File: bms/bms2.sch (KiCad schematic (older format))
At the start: 44 parts

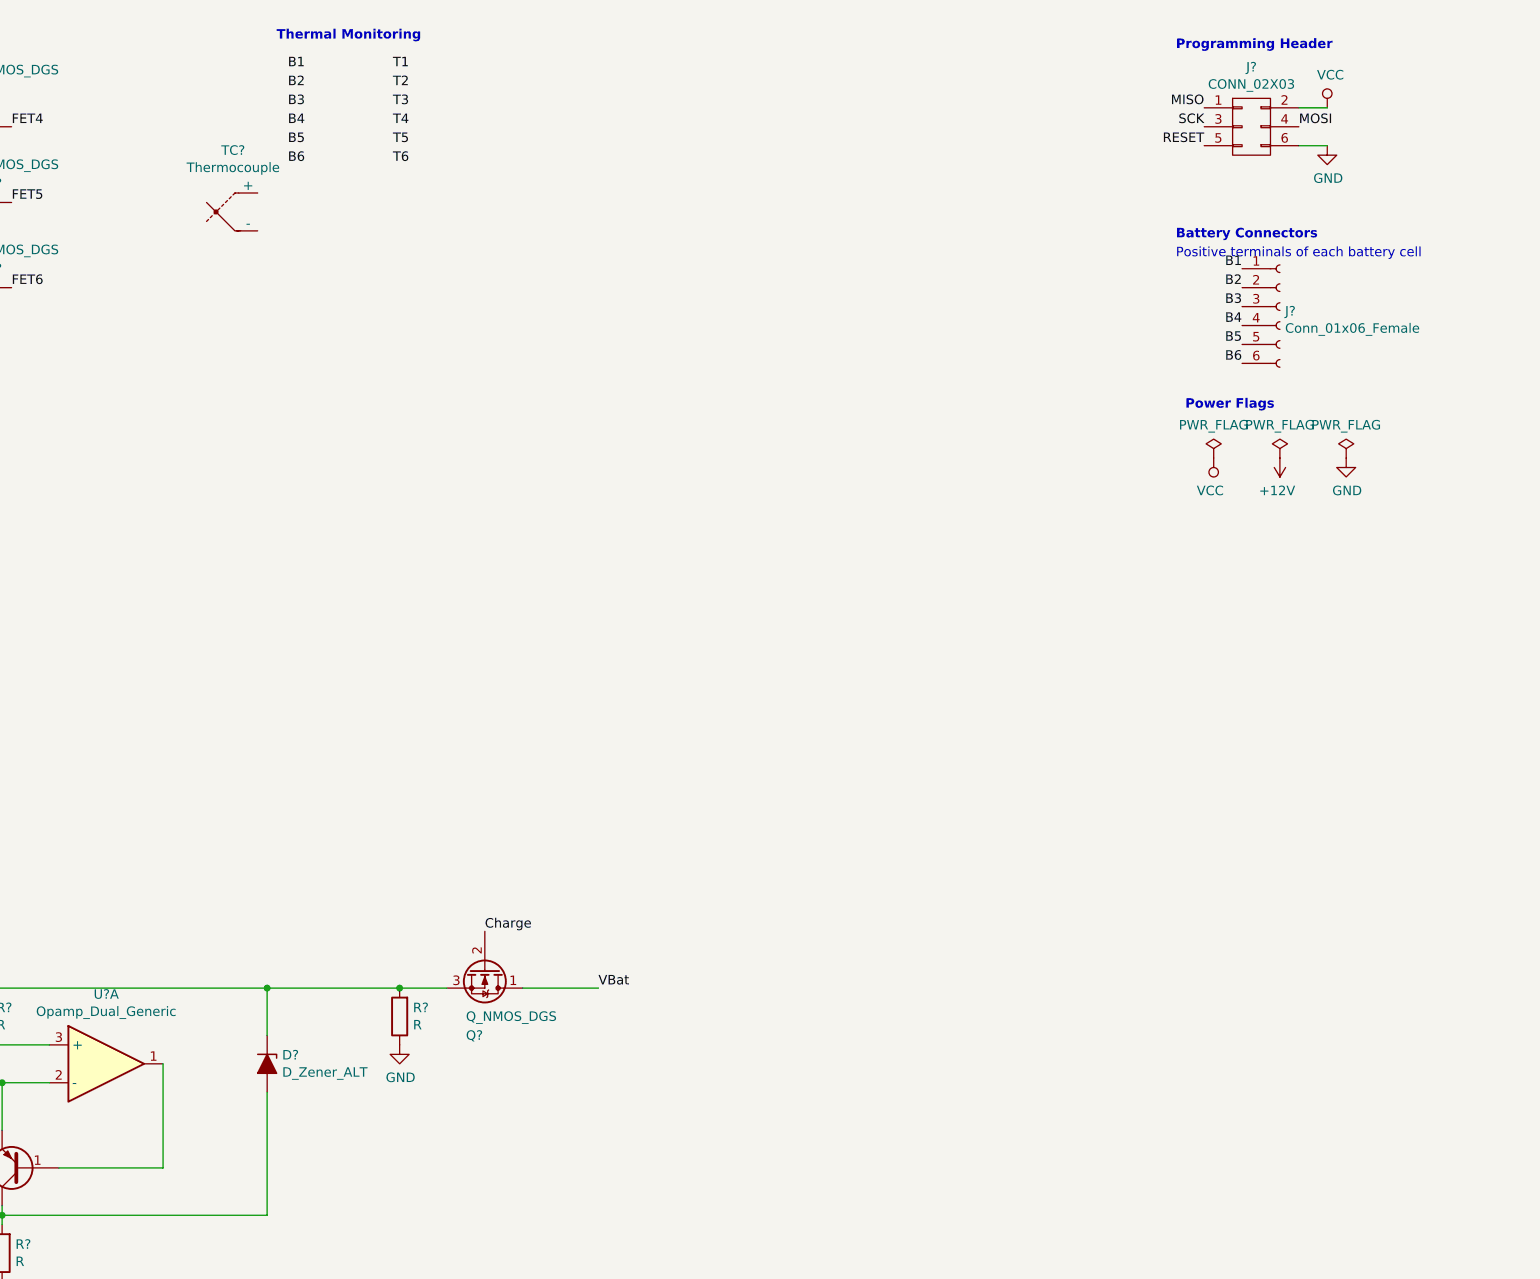
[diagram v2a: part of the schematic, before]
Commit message: thermal monitoring and eFuse safety
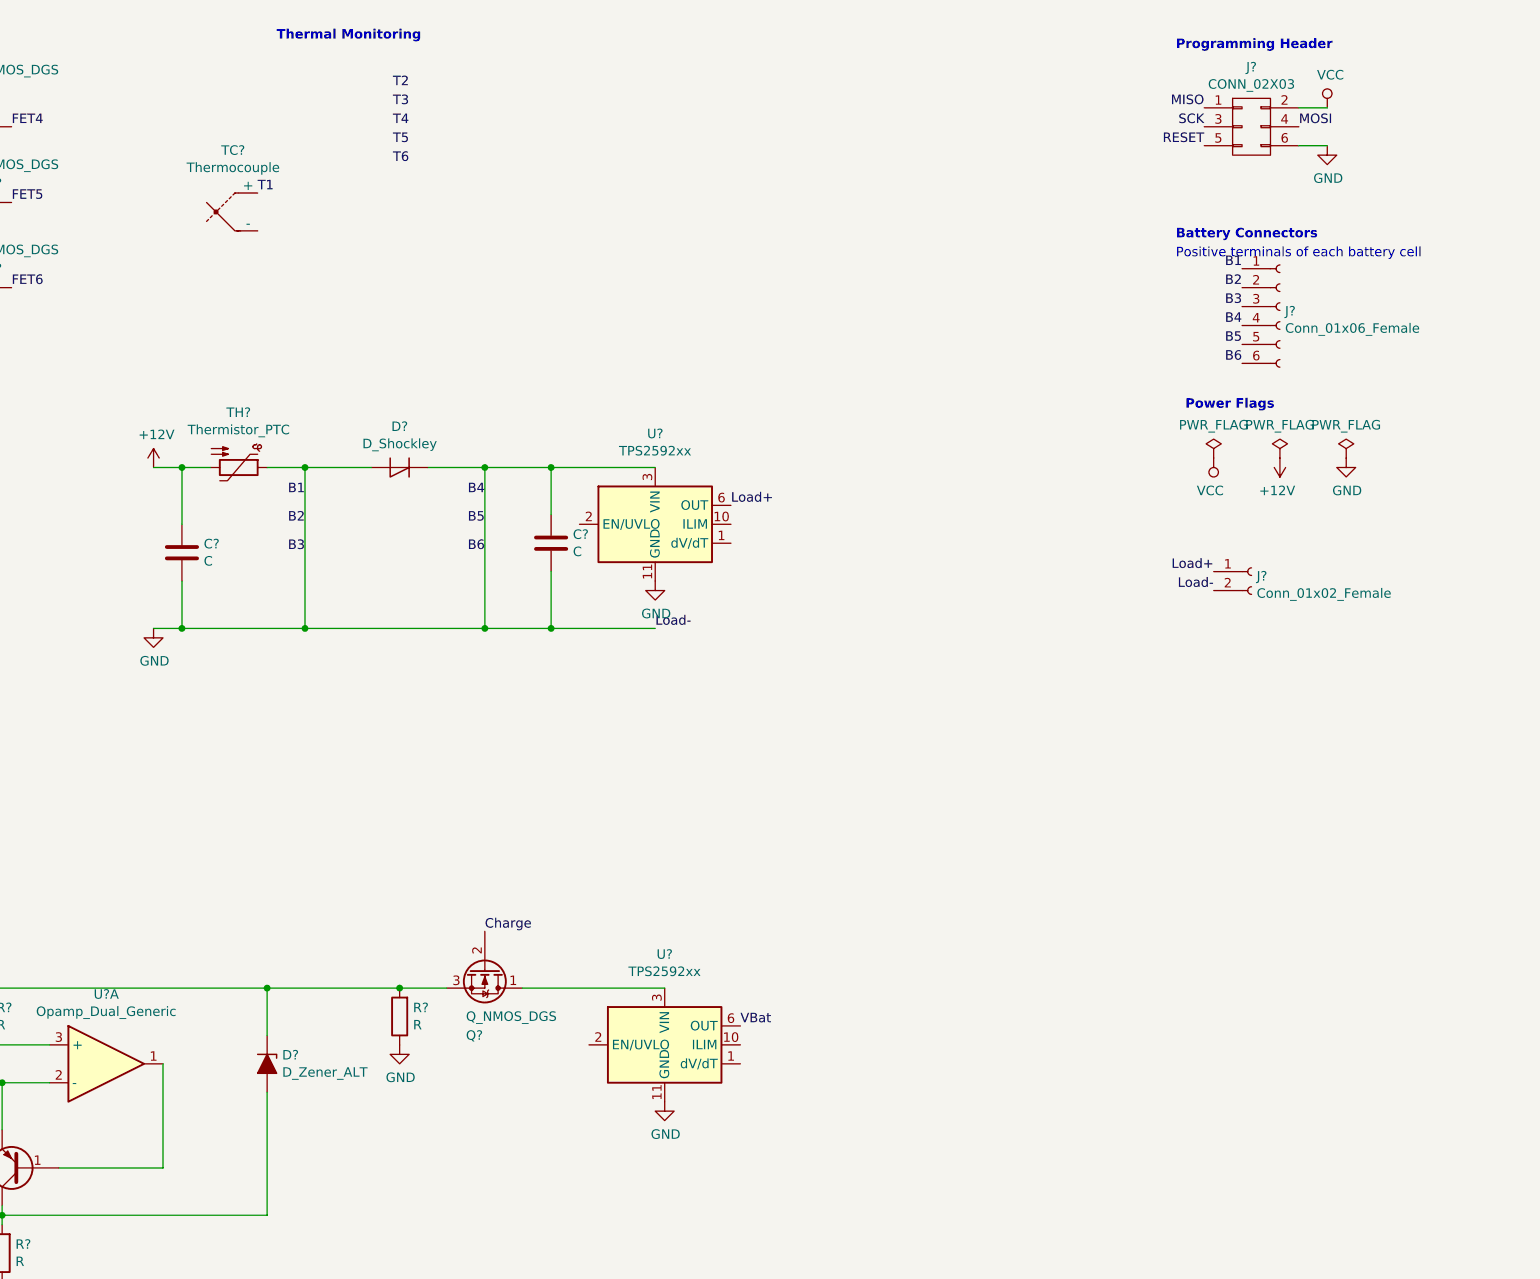
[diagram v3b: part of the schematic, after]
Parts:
- added C? (x2): C, symbol Device:C
- added D?: D_Shockley, symbol Device:D_Shockley
- added J?: Conn_01x02_Female, symbol Connector:Conn_01x02_Female
- added TH?: Thermistor_PTC, symbol Device:Thermistor_PTC
- added U? (x2): TPS2592xx, Package_SON:VSON-10-1EP_3x3mm_P0.5mm_EP1.65x2.4mm_ThermalVias, symbol Power_Management:TPS2592xx
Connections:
- net B1 is gone; now on net GND: J?.1 (Pin_1), R?.2
- net B2 is gone; now on net GND: J?.2 (Pin_2), R?.2
- net B3 is gone; now on net GND: J?.3 (Pin_3), R?.2
- net B4 is gone; now on net GND: J?.4 (Pin_4), R?.2
- net B5 is gone; now on net GND: J?.5 (Pin_5), R?.2
- net B6 is gone; now on net GND: J?.6 (Pin_6), R?.2
- net +12V: now also C?.1, TH?.2
- net GND: now also C?.1, C?.2, C?.2, D?.1 (K), D?.2 (A), J?.2 (Pin_2), TH?.1, U?.11 (GND), U?.11 (GND), U?.3 (VIN), U?.4 (VIN), U?.5 (VIN)
- net T1: now also TC?.1 (+)
- net VBat: now also U?.6 (OUT), U?.7 (OUT), U?.8 (OUT); no longer Q?.1 (D)
- new net: Q?.1 (D), U?.3 (VIN), U?.4 (VIN), U?.5 (VIN)
- new net Load+: J?.1 (Pin_1), U?.6 (OUT), U?.7 (OUT), U?.8 (OUT)
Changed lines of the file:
@@
 Text Notes 950  6450 0    50   ~ 0
 Buck Power Stage\n
-Text Label 6600 5800 0    50   ~ 0
+Text Label 7350 6000 0    50   ~ 0
 VBat
 Text Label 2450 3200 0    50   ~ 0
@@
 Text Label 6000 5500 0    50   ~ 0
 Charge
-Wire Wire Line
-	6200 5800 6600 5800
 Text Notes 4900 800  0    50   ~ 10
 Thermal Monitoring\n
@@
 Text Label 10000 2500 2    50   ~ 0
 B6
-Text Label 5050 950  2    50   ~ 0
-B1
-Text Label 5050 1050 2    50   ~ 0
-B2
-Text Label 5050 1150 2    50   ~ 0
-B3
-Text Label 5050 1250 2    50   ~ 0
-B4
-Text Label 5050 1350 2    50   ~ 0
-B5
-Text Label 5050 1450 2    50   ~ 0
-B6
-Text Label 5600 950  2    50   ~ 0
+Text Label 4800 1600 0    50   ~ 0
 T1
 Text Label 5600 1050 2    50   ~ 0
@@
 	1    0    0    -1
 $EndComp
+Text Label 5050 3200 2    50   ~ 0
+B1
+Text Label 5050 3350 2    50   ~ 0
+B2
+Text Label 5050 3500 2    50   ~ 0
+B3
+Text Label 6000 3200 2    50   ~ 0
+B4
+Text Label 6000 3350 2    50   ~ 0
+B5
+Text Label 6000 3500 2    50   ~ 0
+B6
+Wire Wire Line
+	4250 3050 4400 3050
+Wire Wire Line
+	6000 3050 6350 3050
+Wire Wire Line
+	4250 3900 4400 3900
+Wire Wire Line
+	5050 3050 5050 3900
+Connection ~ 5050 3900
+Wire Wire Line
+	5050 3900 6000 3900
+Wire Wire Line
+	6000 3050 6000 3900
+Connection ~ 6000 3900
+Wire Wire Line
+	6000 3900 6350 3900
+$Comp
+L power:+12V #PWR?
+U 1 1 5E179A7D
+P 4250 3050
+F 0 "#PWR?" H 4250 2900 50  0001 C CNN
+F 1 "+12V" H 4265 3223 50  0000 C CNN
+F 2 "" H 4250 3050 50  0001 C CNN
+F 3 "" H 4250 3050 50  0001 C CNN
+	1    4250 3050
+	1    0    0    -1
+$EndComp
+$Comp
+L power:GND #PWR?
+U 1 1 5E179C4F
+P 4250 3900
+F 0 "#PWR?" H 4250 3650 50  0001 C CNN
+F 1 "GND" H 4255 3727 50  0000 C CNN
+F 2 "" H 4250 3900 50  0001 C CNN
+F 3 "" H 4250 3900 50  0001 C CNN
+	1    4250 3900
+	1    0    0    -1
+$EndComp
+$Comp
+L Connector:Conn_01x02_Female J?
+U 1 1 5E179EB6
+P 10050 3600
+F 0 "J?" H 10077 3576 50  0000 L CNN
+F 1 "Conn_01x02_Female" H 10077 3485 50  0000 L CNN
+F 2 "" H 10050 3600 50  0001 C CNN
+F 3 "~" H 10050 3600 50  0001 C CNN
+	1    10050 3600
+	1    0    0    -1
+$EndComp
+Text Label 9850 3600 2    50   ~ 0
+Load+
+Text Label 9850 3700 2    50   ~ 0
+Load-
+Text Label 7300 3250 0    50   ~ 0
+Load+
+Text Label 6900 3900 0    50   ~ 0
+Load-
+$Comp
+L Device:D_Shockley D?
+U 1 1 5E17A7E8
+P 5550 3050
+F 0 "D?" H 5550 2834 50  0000 C CNN
+F 1 "D_Shockley" H 5550 2925 50  0000 C CNN
+F 2 "" H 5550 3050 50  0001 C CNN
+F 3 "~" H 5550 3050 50  0001 C CNN
+	1    5550 3050
+	-1   0    0    1
+$EndComp
+$Comp
+L power:GND #PWR?
+U 1 1 5E17AAB6
+P 6900 3650
+F 0 "#PWR?" H 6900 3400 50  0001 C CNN
+F 1 "GND" H 6905 3477 50  0000 C CNN
+F 2 "" H 6900 3650 50  0001 C CNN
+F 3 "" H 6900 3650 50  0001 C CNN
+	1    6900 3650
+	1    0    0    -1
+$EndComp
+$Comp
+L Power_Management:TPS2592xx U?
+U 1 1 5E17AB1F
+P 6900 3350
+F 0 "U?" H 6900 3828 50  0000 C CNN
+F 1 "TPS2592xx" H 6900 3737 50  0000 C CNN
+F 2 "Package_SON:VSON-10-1EP_3x3mm_P0.5mm_EP1.65x2.4mm_ThermalVias" H 6850 2700 50  0001 C CNN
+F 3 "http://www.ti.com/lit/ds/symlink/tps25925.pdf" H 6500 3750 50  0001 C CNN
+	1    6900 3350
+	1    0    0    -1
+$EndComp
+Wire Wire Line
+	5050 3050 5400 3050
+Wire Wire Line
+	5700 3050 6000 3050
+Connection ~ 5050 3050
+Connection ~ 6000 3050
+$Comp
+L Power_Management:TPS2592xx U?
+U 1 1 5E17D9BC
+P 6950 6100
+F 0 "U?" H 6950 6578 50  0000 C CNN
+F 1 "TPS2592xx" H 6950 6487 50  0000 C CNN
+F 2 "Package_SON:VSON-10-1EP_3x3mm_P0.5mm_EP1.65x2.4mm_ThermalVias" H 6900 5450 50  0001 C CNN
+F 3 "http://www.ti.com/lit/ds/symlink/tps25925.pdf" H 6550 6500 50  0001 C CNN
+	1    6950 6100
+	1    0    0    -1
+$EndComp
+Wire Wire Line
+	6200 5800 6950 5800
+$Comp
+L power:GND #PWR?
+U 1 1 5E1803FE
+P 6950 6400
+F 0 "#PWR?" H 6950 6150 50  0001 C CNN
+F 1 "GND" H 6955 6227 50  0000 C CNN
+F 2 "" H 6950 6400 50  0001 C CNN
+F 3 "" H 6950 6400 50  0001 C CNN
+	1    6950 6400
+	1    0    0    -1
+$EndComp
+$Comp
+L Device:C C?
+U 1 1 5E18086C
+P 4400 3500
+F 0 "C?" H 4515 3546 50  0000 L CNN
+F 1 "C" H 4515 3455 50  0000 L CNN
+F 2 "" H 4438 3350 50  0001 C CNN
+F 3 "~" H 4400 3500 50  0001 C CNN
+	1    4400 3500
+	1    0    0    -1
+$EndComp
+$Comp
+L Device:C C?
+U 1 1 5E18097C
+P 6350 3450
+F 0 "C?" H 6465 3496 50  0000 L CNN
+F 1 "C" H 6465 3405 50  0000 L CNN
+F 2 "" H 6388 3300 50  0001 C CNN
+F 3 "~" H 6350 3450 50  0001 C CNN
+	1    6350 3450
+	1    0    0    -1
+$EndComp
+$Comp
+L Device:Thermistor_PTC TH?
+U 1 1 5E180AA9
+P 4700 3050
+F 0 "TH?" V 4410 3050 50  0000 C CNN
+F 1 "Thermistor_PTC" V 4501 3050 50  0000 C CNN
+F 2 "" H 4750 2850 50  0001 L CNN
+F 3 "~" H 4700 3050 50  0001 C CNN
+	1    4700 3050
+	0    1    1    0
+$EndComp
+Wire Wire Line
+	6350 3050 6350 3300
+Wire Wire Line
+	6350 3600 6350 3900
+Connection ~ 6350 3050
+Wire Wire Line
+	6350 3050 6900 3050
+Connection ~ 6350 3900
+Wire Wire Line
+	6350 3900 6900 3900
+Wire Wire Line
+	4400 3050 4400 3350
+Wire Wire Line
+	4400 3650 4400 3900
+Connection ~ 4400 3050
+Wire Wire Line
+	4400 3050 4550 3050
+Connection ~ 4400 3900
+Wire Wire Line
+	4400 3900 5050 3900
+Wire Wire Line
+	4850 3050 5050 3050
 $EndSCHEMATC

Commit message: MAX1648 charging chip!
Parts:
- added C? (x2): CP, symbol Device:CP
- added C? (x5): C, symbol Device:C
- added D?: D_Shockley, symbol Device:D_Shockley
- added D? (x3): D_Schottky, symbol Device:D_Schottky
- added D?: D, symbol Device:D
- added L?: INDUCTOR, symbol pspice:INDUCTOR
- added M? (x2): MNMOS, symbol pspice:MNMOS
- added Q?: BS170, Package_TO_SOT_THT:TO-92_Inline, symbol Transistor_FET:BS170
- added R? (x9): R, symbol Device:R
- added TC? (x5): Thermocouple, symbol Device:Thermocouple
- added U?: ATSAMD21G18A-AUT, digikey-footprints:TQFP-48_7x7mm, symbol dk_Embedded-Microcontrollers:ATSAMD21G18A-AUT
- added U?: MAX1648, Package_SO:SOIC-16_3.9x9.9mm_P1.27mm, symbol Battery_Management:MAX1648
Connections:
- net labels added: LoadSwitch, SafetySwitch
- wire segments 99 -> 165
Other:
- note added: "Load Switch\n"
- moved on the sheet: C?, D?, J?, L?, Q?, R?, TC?, TH?, U?, U?A

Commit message: C and R values for charging circuit
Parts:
- removed C? (x3): C, symbol Device:C
- removed D?: D, symbol Device:D
- removed D?: D_Zener_ALT, symbol Device:D_Zener_ALT
- removed L?: INDUCTOR, symbol pspice:INDUCTOR
- removed Q?: Q_PNP_BCE, symbol Device:Q_PNP_BCE
- removed Q?: Q_NMOS_DGS, symbol Device:Q_NMOS_DGS
- removed Q?: BS170, Package_TO_SOT_THT:TO-92_Inline, symbol Transistor_FET:BS170
- removed R? (x5): R, symbol Device:R
- removed TC? (x6): Thermocouple, symbol Device:Thermocouple
- removed TH?: Thermistor_PTC, symbol Device:Thermistor_PTC
- removed U?: Opamp_Dual_Generic, symbol Device:Opamp_Dual_Generic
- removed U?: TPS2592xx, Package_SON:VSON-10-1EP_3x3mm_P0.5mm_EP1.65x2.4mm_ThermalVias, symbol Power_Management:TPS2592xx
- added C10: 0.1uF, Capacitor_SMD:C_0805_2012Metric_Pad1.15x1.40mm_HandSolder, symbol Device:C_Small
- added C17: CP1, Capacitor_SMD:C_0805_2012Metric_Pad1.15x1.40mm_HandSolder, symbol Device:CP1
- added J2: Conn_01x02_Female, Connector_PinHeader_1.00mm:PinHeader_1x02_P1.00mm_Vertical, symbol Connector:Conn_01x02_Female
- added Q4, Q8: Q_NMOS_DGS, symbol Device:Q_NMOS_DGS
- added R11, R12, R14, R20, R21, R23, R26, R27, R29: R, Resistor_SMD:R_0805_2012Metric_Pad1.15x1.40mm_HandSolder, symbol Device:R
- added TH1, TH2, TH3, TH4, TH5, TH6, TH7: Thermistor, symbol Device:Thermistor
- C1, C12, C13, C14, C15, C16, C5, C6, C7: renamed from C?; footprint (none) -> Capacitor_SMD:C_0805_2012Metric_Pad1.15x1.40mm_HandSolder
- C11: renamed from C?; value CP -> 47uF; footprint (none) -> Capacitor_SMD:C_0805_2012Metric_Pad1.15x1.40mm_HandSolder
- C2, C4: renamed from C?; value C -> 0.1uF; footprint (none) -> Capacitor_SMD:C_0805_2012Metric_Pad1.15x1.40mm_HandSolder
- C3: renamed from C?; value C -> 47nF; footprint (none) -> Capacitor_SMD:C_0805_2012Metric_Pad1.15x1.40mm_HandSolder
- C8: renamed from C?; value CP -> 22uF; footprint (none) -> Capacitor_SMD:C_0805_2012Metric_Pad1.15x1.40mm_HandSolder
- C9: renamed from C?; value C -> 1uF; footprint (none) -> Capacitor_SMD:C_0805_2012Metric_Pad1.15x1.40mm_HandSolder
- D3, D5, D6: renamed from D?; value D_Schottky -> S
- D4: renamed from D?; value D -> FR
- J1: renamed from J?; footprint (none) -> Connector_PinHeader_1.00mm:PinHeader_1x02_P1.00mm_Vertical
- J4: renamed from J?; footprint (none) -> Connector_PinHeader_1.00mm:PinHeader_1x06_P1.00mm_Vertical
- L1: renamed from L?; value INDUCTOR -> 22uH; footprint (none) -> Inductor_SMD:L_0805_2012Metric_Pad1.15x1.40mm_HandSolder
- M1: renamed from M?; value MNMOS -> 10
- M2: renamed from M?; value MNMOS -> 0.1
- R1, R10, R16, R17, R18, R19, R2, R24, R25, R28, R3, R4, R7, R8, R9: renamed from R?; footprint (none) -> Resistor_SMD:R_0805_2012Metric_Pad1.15x1.40mm_HandSolder
- R13, R22, R5, R6: renamed from R?; value R -> 10k; footprint (none) -> Resistor_SMD:R_0805_2012Metric_Pad1.15x1.40mm_HandSolder
- R15: renamed from R?; value R -> 10; footprint (none) -> Resistor_SMD:R_0805_2012Metric_Pad1.15x1.40mm_HandSolder
- gave numbers to parts that had none: 16
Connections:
- net labels added: BAT+, BAT-, DC+, DC-, LOAD+, LOAD-
- net labels removed: Charge, Load+, Load-, LoadSwitch, VBat
- wire segments 165 -> 192
- no-connect marks 0 -> 24
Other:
- note added: "Charging\n"
- note removed: "Buck Power Stage\n"
- note removed: "CC/CV Charging"
- note removed: "Load Switch\n"
- moved on the sheet: C1, C11, C12, C13, C14, C15, C16, C2, C3, C4, C5, C6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

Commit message: all footprints addedgit add .git add .!
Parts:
- removed D4: FR, symbol Device:D
- removed M1: 10, symbol pspice:MNMOS
- removed M2: 0.1, symbol pspice:MNMOS
- removed Q1, Q2, Q3, Q4, Q5, Q6, Q7, Q8, Q9: Q_NMOS_DGS, symbol Device:Q_NMOS_DGS
- removed Q10: Q_NMOS_SGD, symbol Device:Q_NMOS_SGD
- removed U3: Opamp_Dual_Generic, symbol Device:Opamp_Dual_Generic
- added D4: UF5400, Diode_THT:D_DO-201AD_P15.24mm_Horizontal, symbol Diode:UF5400
- added Q1, Q10, Q11, Q2, Q3, Q4, Q5, Q6, Q7, Q8, Q9: BS170, Package_TO_SOT_THT:TO-92_Inline, symbol Transistor_FET:BS170
- added Q12: BSB014N04LX3, Package_DirectFET:DirectFET_MX, symbol Transistor_FET:BSB014N04LX3
- added U3: LMC6482, footprints:SOIC127P600X175-8N, symbol Amplifier_Operational:LMC6482
- D1, D2, D3, D5, D6: footprint (none) -> footprints:SD103AW-13-F
- D7: footprint (none) -> LED_SMD:LED_0805_2012Metric_Pad1.15x1.40mm_HandSolder
- TH1, TH2, TH3, TH4, TH5, TH6, TH7: footprint (none) -> footprints:Thermistor
- U4: footprint digikey-footprints:TQFP-48_7x7mm -> footprints:TO-263-2-Heatsink
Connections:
- net +12V: now also U3.2 (-)
- net B1: now also Q4.1 (D)
- net B4: now also Q8.1 (D), Q9.1 (D)
- net Discharge: now also Q9.2 (G)
- net FET1: now also Q1.2 (G)
- net FET2: now also Q2.2 (G)
- net FET3: now also Q3.2 (G)
- net FET4: now also Q5.2 (G)
- net FET5: now also Q6.2 (G)
- net FET6: now also Q7.2 (G)
- net GND: now also Q11.3 (S), Q4.3 (S), Q8.3 (S)
- net SafetySwitch: now also Q4.2 (G), Q8.2 (G)
- net at C16.2, R25.1: now also U3.1
- net at C16.1, R28.1: now also U3.3 (+)
- net at D7.1 (K): now also Q10.3 (S)
- net at D7.2 (A): now also Q9.3 (S)
- net at R25.2: now also Q10.2 (G)
- net at R24.2, R28.2: now also Q10.1 (D)
- net at C5.1, R7.1: now also Q1.1 (D)
- net at C5.2, C6.1, R8.1: now also Q1.3 (S), Q2.1 (D)
- net at C6.2, C7.1, R9.1: now also Q2.3 (S), Q3.1 (D)
- net at C7.2, R10.1: now also Q3.3 (S)
- net at C12.1, R16.1: now also Q5.1 (D)
- net at C12.2, C13.1, R17.1: now also Q5.3 (S), Q6.1 (D)
- net at C13.2, C14.1, R18.1: now also Q6.3 (S), Q7.1 (D)
- net at C14.2, R19.1: now also Q7.3 (S)
- net at C8.1, D5.1 (K), U1.1 (DCIN): now also Q12.1 (D)
- net at U1.13 (DLO): now also Q11.2 (G)
- net at U1.14 (DHI): now also Q12.2 (G)
- net at C10.2, D3.1 (K), L1.1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: now also Q11.1 (D), Q12.3 (S)
- net at C10.1, U1.16 (BST): now also D4.1 (K)
- net at R15.1: now also D4.2 (A)
